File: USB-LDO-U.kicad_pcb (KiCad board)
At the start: 2 copper layers, 20 x 13 mm, 7 parts, among them J1 USB_B_Micro, J2 Conn_01x05_Pin, U1 AMS1117-3.3

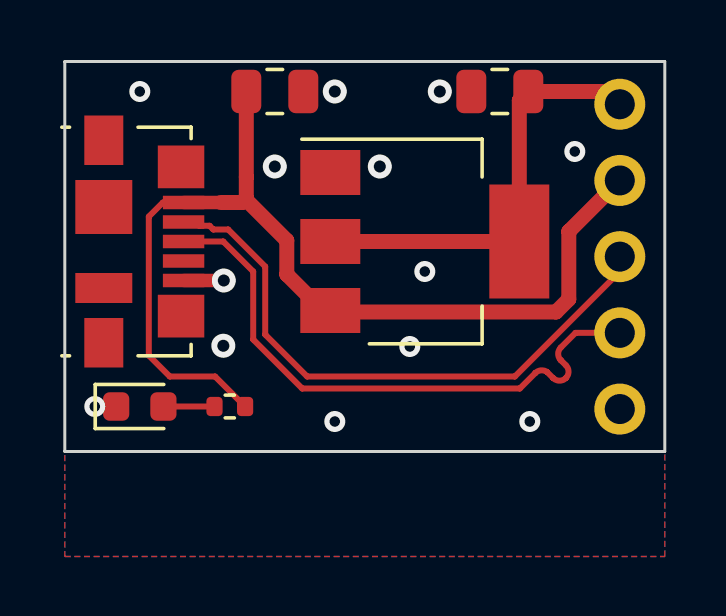
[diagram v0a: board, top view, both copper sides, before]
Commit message: Rounded board corners. Moved texts around.
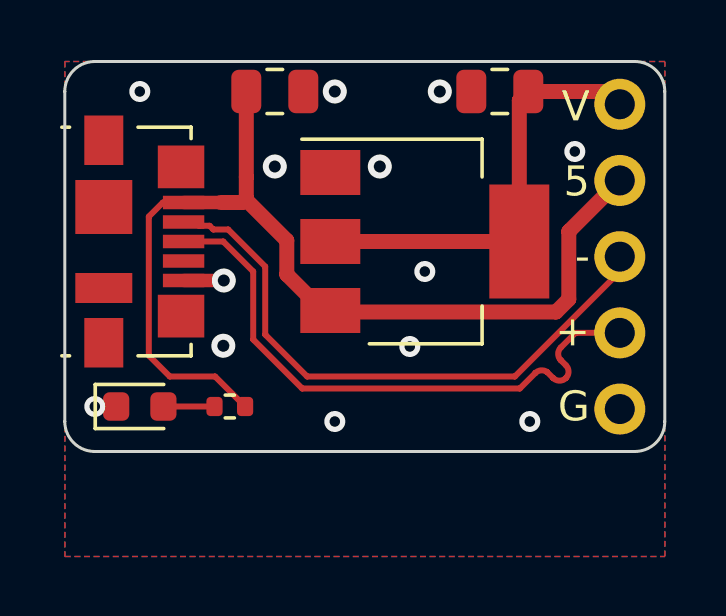
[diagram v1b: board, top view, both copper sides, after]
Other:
- outline, holes or cut-outs redrawn
- board text added: "+"
- board text added: "-"
- board text added: "5"
- board text added: "G"
- board text added: "V"
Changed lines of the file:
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@@
     )
   )
-  (gr_line (start 170 106.5) (end 170 93.5)
+  (gr_line (start 170 105.5) (end 170 94.5)
     (stroke (width 0.1) (type default)) (layer "Edge.Cuts"))
-  (gr_line (start 170 106.5) (end 150 106.5)
+  (gr_line (start 169 106.5) (end 151 106.5)
     (stroke (width 0.1) (type default)) (layer "Edge.Cuts"))
-  (gr_line (start 150 106.5) (end 150 93.5)
+  (gr_arc (start 150 94.5) (mid 150.292893 93.792893) (end 151 93.5)
     (stroke (width 0.1) (type default)) (layer "Edge.Cuts"))
-  (gr_line (start 170 93.5) (end 150 93.5)
+  (gr_arc (start 151 106.5) (mid 150.292893 106.207107) (end 150 105.5)
     (stroke (width 0.1) (type default)) (layer "Edge.Cuts"))
-  (gr_text "${TITLE}" (at 157.5 98.5) (layer "B.SilkS")
+  (gr_arc (start 169 93.5) (mid 169.707107 93.792893) (end 170 94.5)
+    (stroke (width 0.1) (type default)) (layer "Edge.Cuts"))
+  (gr_line (start 150 105.5) (end 150 94.5)
+    (stroke (width 0.1) (type default)) (layer "Edge.Cuts"))
+  (gr_line (start 169 93.5) (end 151 93.5)
+    (stroke (width 0.1) (type default)) (layer "Edge.Cuts"))
+  (gr_arc (start 170 105.5) (mid 169.707107 106.207107) (end 169 106.5)
+    (stroke (width 0.1) (type default)) (layer "Edge.Cuts"))
+  (gr_text "${TITLE}" (at 158 98.5) (layer "B.SilkS")
     (effects (font (size 1 1) (thickness 0.15)) (justify mirror))
   )
-  (gr_text "D-" (at 167 100) (layer "B.SilkS")
+  (gr_text "D-" (at 167.5 100) (layer "B.SilkS")
     (effects (font (size 1 1) (thickness 0.15)) (justify left mirror))
   )
-  (gr_text "GND" (at 167 105) (layer "B.SilkS")
+  (gr_text "GND" (at 167.5 105) (layer "B.SilkS")
     (effects (font (size 1 1) (thickness 0.15)) (justify left mirror))
   )
-  (gr_text "D+" (at 167 102.5) (layer "B.SilkS")
+  (gr_text "D+" (at 167.5 102.5) (layer "B.SilkS")
     (effects (font (size 1 1) (thickness 0.15)) (justify left mirror))
   )
-  (gr_text "VCC" (at 167 95) (layer "B.SilkS")
+  (gr_text "VCC" (at 167.5 95) (layer "B.SilkS")
     (effects (font (size 1 1) (thickness 0.15)) (justify left mirror))
   )
-  (gr_text "5V" (at 167 97.5) (layer "B.SilkS")
+  (gr_text "5V" (at 167.5 97.5) (layer "B.SilkS")
     (effects (font (size 1 1) (thickness 0.15)) (justify left mirror))
   )
-  (gr_text "${COMPANY}" (at 157.5 101.5) (layer "B.SilkS")
+  (gr_text "${COMPANY}" (at 158 101.5) (layer "B.SilkS")
     (effects (font (size 1 1) (thickness 0.15)) (justify mirror))
   )
+  (gr_text "V" (at 167.5 95) (layer "F.SilkS")
+    (effects (font (size 1 1) (thickness 0.15)) (justify right))
+  )
+  (gr_text "+" (at 167.5 102.5) (layer "F.SilkS")
+    (effects (font (size 1 1) (thickness 0.15)) (justify right))
+  )
+  (gr_text "5" (at 167.5 97.5) (layer "F.SilkS")
+    (effects (font (size 1 1) (thickness 0.15)) (justify right))
+  )
+  (gr_text "-" (at 167.5 100) (layer "F.SilkS")
+    (effects (font (size 1 1) (thickness 0.15)) (justify right))
+  )
+  (gr_text "G" (at 167.5 105) (layer "F.SilkS")
+    (effects (font (size 1 1) (thickness 0.15)) (justify right))
+  )
   (segment (start 157.4 100.6) (end 157.4 99.465293) (width 0.5) (layer "F.Cu") (net 1))
